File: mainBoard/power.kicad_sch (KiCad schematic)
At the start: 5 parts

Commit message: LEDky, měření napájení, připojení DRV atd.
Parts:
- gave numbers to parts that had none: 5

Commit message: WIP
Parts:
- C3: footprint Inductor_SMD:L_0805_2012Metric -> Inductor_SMD:L_0402_1005Metric; LCSC C385977 -> C52923
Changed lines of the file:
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@@
       (effects (font (size 1.27 1.27)) (justify left))
     )
-    (property "Footprint" "Inductor_SMD:L_0805_2012Metric" (at 138.1252 104.14 0)
+    (property "Footprint" "Inductor_SMD:L_0402_1005Metric" (at 138.1252 104.14 0)
       (effects (font (size 1.27 1.27)) hide)
     )
@@
       (effects (font (size 1.27 1.27)) hide)
     )
-    (property "LCSC" "C385977" (at 137.16 100.33 0)
+    (property "LCSC" "C52923" (at 137.16 100.33 0)
       (effects (font (size 1.27 1.27)) hide)
     )

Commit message: WIP
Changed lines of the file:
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@@
+    (stroke (width 0) (type default))
+  )
+  (wire (pts (xy 177.8 81.28) (xy 177.8 83.82))
     (stroke (width 0) (type default))
   )
@@
         )
       )
+    )
+  )
+  (symbol (lib_id "power:PWR_FLAG") (at 177.8 81.28 0) (unit 1)
+    (in_bom yes) (on_board yes) (dnp no) (fields_autoplaced)
+    (property "Reference" "#FLG01" (at 177.8 79.375 0)
+      (effects (font (size 1.27 1.27)) hide)
+    )
+    (property "Value" "PWR_FLAG" (at 177.8 76.2 0)
+      (effects (font (size 1.27 1.27)))
+    )
+    (property "Footprint" "" (at 177.8 81.28 0)
+      (effects (font (size 1.27 1.27)) hide)
+    )
+    (property "Datasheet" "~" (at 177.8 81.28 0)
+      (effects (font (size 1.27 1.27)) hide)
+    )
+    (pin "1")
+    (instances
+      (project "mainBoard"
+        (path "/30ed06d7-0b03-4878-b461-066cda7e7438/64dbc0d3-4eed-460b-93d3-a846dd72318b"
+          (reference "#FLG01") (unit 1)
+        )
+      )

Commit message: Moc kondíků
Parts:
- C2: value 1u -> 2u2; footprint Inductor_SMD:L_0805_2012Metric -> Capacitor_SMD:C_0805_2012Metric; LCSC C385977 -> C6119935
- C3: footprint Inductor_SMD:L_0402_1005Metric -> Capacitor_SMD:C_0402_1005Metric
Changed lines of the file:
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@@
+      (effects (font (size 1.27 1.27)) hide)
+    )
+    (property "note" "" (at 152.4 88.9 0)
       (effects (font (size 1.27 1.27)) hide)
     )
@@
       (effects (font (size 1.27 1.27)) (justify left))
     )
-    (property "Footprint" "Inductor_SMD:L_0402_1005Metric" (at 138.1252 104.14 0)
+    (property "Footprint" "Capacitor_SMD:C_0402_1005Metric" (at 138.1252 104.14 0)
       (effects (font (size 1.27 1.27)) hide)
     )
@@
     )
     (property "LCSC" "C52923" (at 137.16 100.33 0)
+      (effects (font (size 1.27 1.27)) hide)
+    )
+    (property "note" "" (at 137.16 100.33 0)
       (effects (font (size 1.27 1.27)) hide)
     )
@@
       (effects (font (size 1.27 1.27)) hide)
     )
+    (property "note" "" (at 171.45 83.82 0)
+      (effects (font (size 1.27 1.27)) hide)
+    )
     (pin "1")
     (pin "2")
@@
     )
     (property "LCSC" "C576470" (at 177.8 95.25 0)
+      (effects (font (size 1.27 1.27)) hide)
+    )
+    (property "note" "" (at 177.8 95.25 0)
       (effects (font (size 1.27 1.27)) hide)
     )
@@
       (effects (font (size 1.27 1.27)) (justify left))
     )
-    (property "Value" "1u" (at 130.81 101.5999 0)
+    (property "Value" "2u2" (at 130.81 101.5999 0)
       (effects (font (size 1.27 1.27)) (justify left))
     )
-    (property "Footprint" "Inductor_SMD:L_0805_2012Metric" (at 127.9652 104.14 0)
+    (property "Footprint" "Capacitor_SMD:C_0805_2012Metric" (at 127.9652 104.14 0)
       (effects (font (size 1.27 1.27)) hide)
     )
@@
       (effects (font (size 1.27 1.27)) hide)
     )
-    (property "LCSC" "C385977" (at 127 100.33 0)
+    (property "LCSC" "C6119935" (at 127 100.33 0)
       (effects (font (size 1.27 1.27)) hide)
     )
+    (property "note" "" (at 127 100.33 0)
+      (effects (font (size 1.27 1.27)) hide)
+    )

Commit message: drobeček
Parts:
- C2: footprint Capacitor_SMD:C_0805_2012Metric -> Capacitor_SMD:C_0402_1005Metric; LCSC C6119935 -> C237392; note (none) -> 35V, X5R
- C4: LCSC C576470 -> C194427; note (none) -> 35V, X5R
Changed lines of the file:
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@@
       (effects (font (size 1.27 1.27)) hide)
     )
-    (property "LCSC" "C576470" (at 177.8 95.25 0)
+    (property "LCSC" "C194427" (at 177.8 95.25 0)
       (effects (font (size 1.27 1.27)) hide)
     )
-    (property "note" "" (at 177.8 95.25 0)
+    (property "note" "35V, X5R" (at 177.8 95.25 0)
       (effects (font (size 1.27 1.27)) hide)
     )
@@
       (effects (font (size 1.27 1.27)) (justify left))
     )
-    (property "Footprint" "Capacitor_SMD:C_0805_2012Metric" (at 127.9652 104.14 0)
+    (property "Footprint" "Capacitor_SMD:C_0402_1005Metric" (at 127.9652 104.14 0)
       (effects (font (size 1.27 1.27)) hide)
     )
@@
       (effects (font (size 1.27 1.27)) hide)
     )
-    (property "LCSC" "C6119935" (at 127 100.33 0)
+    (property "LCSC" "C237392" (at 127 100.33 0)
       (effects (font (size 1.27 1.27)) hide)
     )
-    (property "note" "" (at 127 100.33 0)
+    (property "note" "35V, X5R" (at 127 100.33 0)
       (effects (font (size 1.27 1.27)) hide)
     )

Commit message: ukild
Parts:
- renumbered C4 to C15, C2 to C16, C3 to C17, U1 to U3
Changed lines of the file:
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@@
   (symbol (lib_id "Regulator_Switching:MAX15062A") (at 152.4 88.9 0) (unit 1)
     (in_bom yes) (on_board yes) (dnp no) (fields_autoplaced)
-    (property "Reference" "U1" (at 152.4 76.2 0)
+    (property "Reference" "U3" (at 152.4 76.2 0)
       (effects (font (size 1.27 1.27)))
     )
@@
   (symbol (lib_id "Device:C") (at 137.16 100.33 0) (unit 1)
     (in_bom yes) (on_board yes) (dnp no) (fields_autoplaced)
-    (property "Reference" "C3" (at 140.97 99.0599 0)
+    (property "Reference" "C17" (at 140.97 99.0599 0)
       (effects (font (size 1.27 1.27)) (justify left))
     )
@@
   (symbol (lib_id "Device:C") (at 177.8 95.25 0) (unit 1)
     (in_bom yes) (on_board yes) (dnp no) (fields_autoplaced)
-    (property "Reference" "C4" (at 181.61 93.9799 0)
+    (property "Reference" "C15" (at 181.61 93.9799 0)
       (effects (font (size 1.27 1.27)) (justify left))
     )
@@
   (symbol (lib_id "Device:C") (at 127 100.33 0) (unit 1)
     (in_bom yes) (on_board yes) (dnp no) (fields_autoplaced)
-    (property "Reference" "C2" (at 130.81 99.0599 0)
+    (property "Reference" "C16" (at 130.81 99.0599 0)
       (effects (font (size 1.27 1.27)) (justify left))
     )

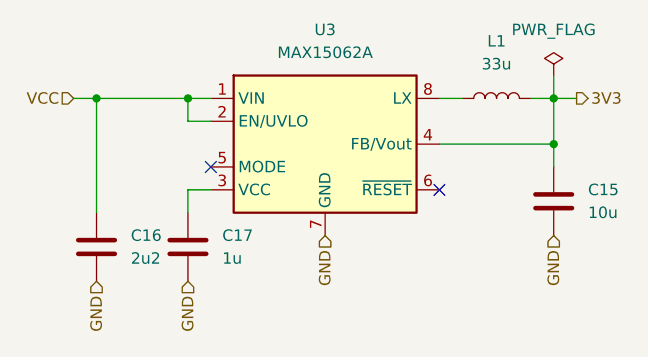
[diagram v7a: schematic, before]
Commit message: Kicad 8 and SDA pullup
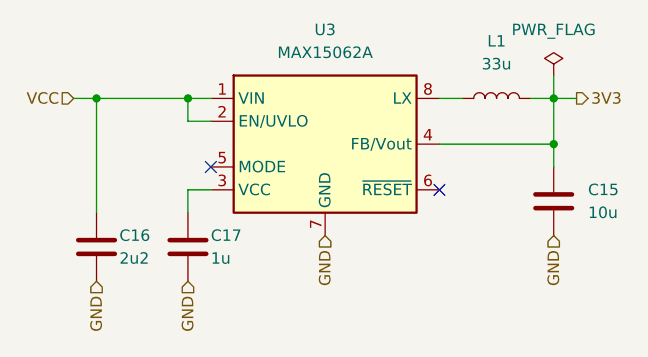
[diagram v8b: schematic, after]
